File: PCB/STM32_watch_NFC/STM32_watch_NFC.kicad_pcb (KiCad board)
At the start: 4 copper layers, 40 x 40 mm, 107 parts, among them J1 Conn_01x06_Socket, J2 USB_C_Receptacle_PowerOnly_6P, Q1 2N7000, SW1 SW_DPST_x2, SW2 SW_DPST_x2, SW3 SW_DPST_x2, U1 STM32L031G6Ux, U2 MIC5365-3.3YC5, U3 ST25R3916-AQWT, U4 MT3608, Y1 27.12Mhz, Y2 32.768kHz

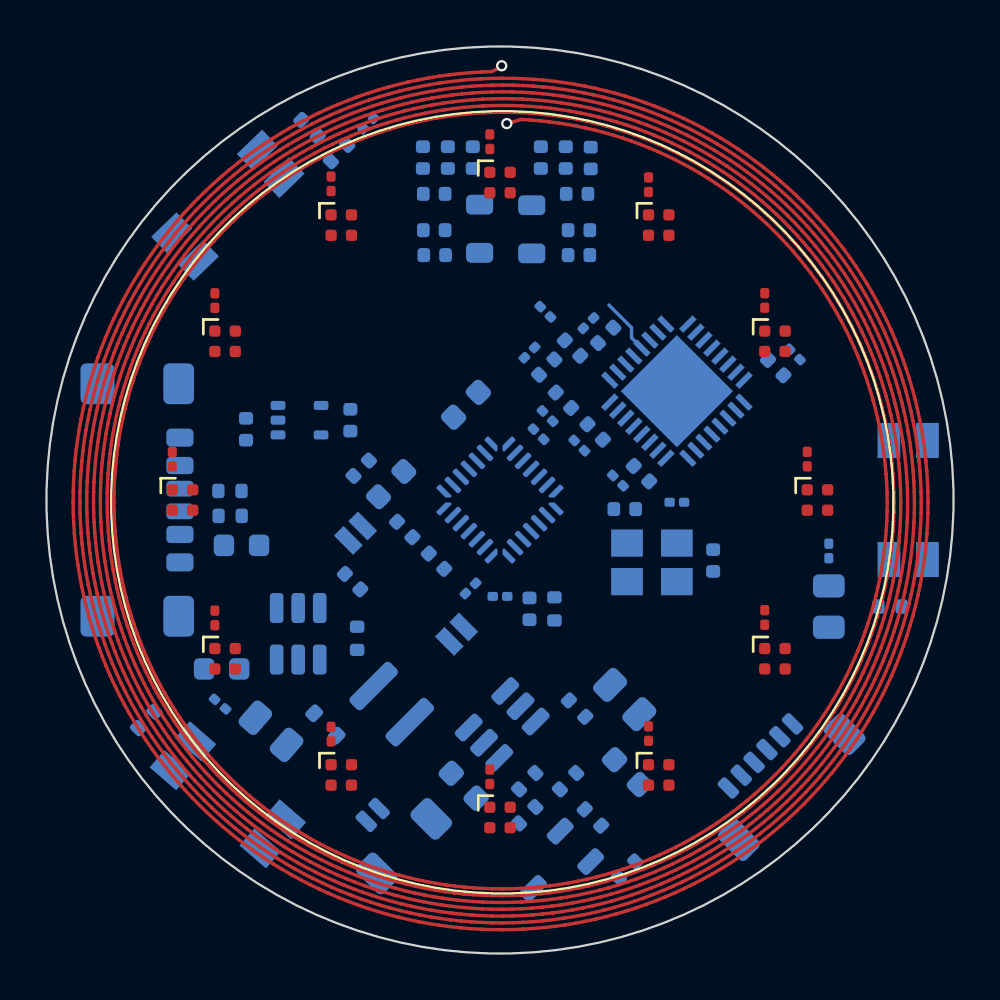
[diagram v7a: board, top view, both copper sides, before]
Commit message: Kicad - Routing 1
Starting routing. I did already a little bitte of routing
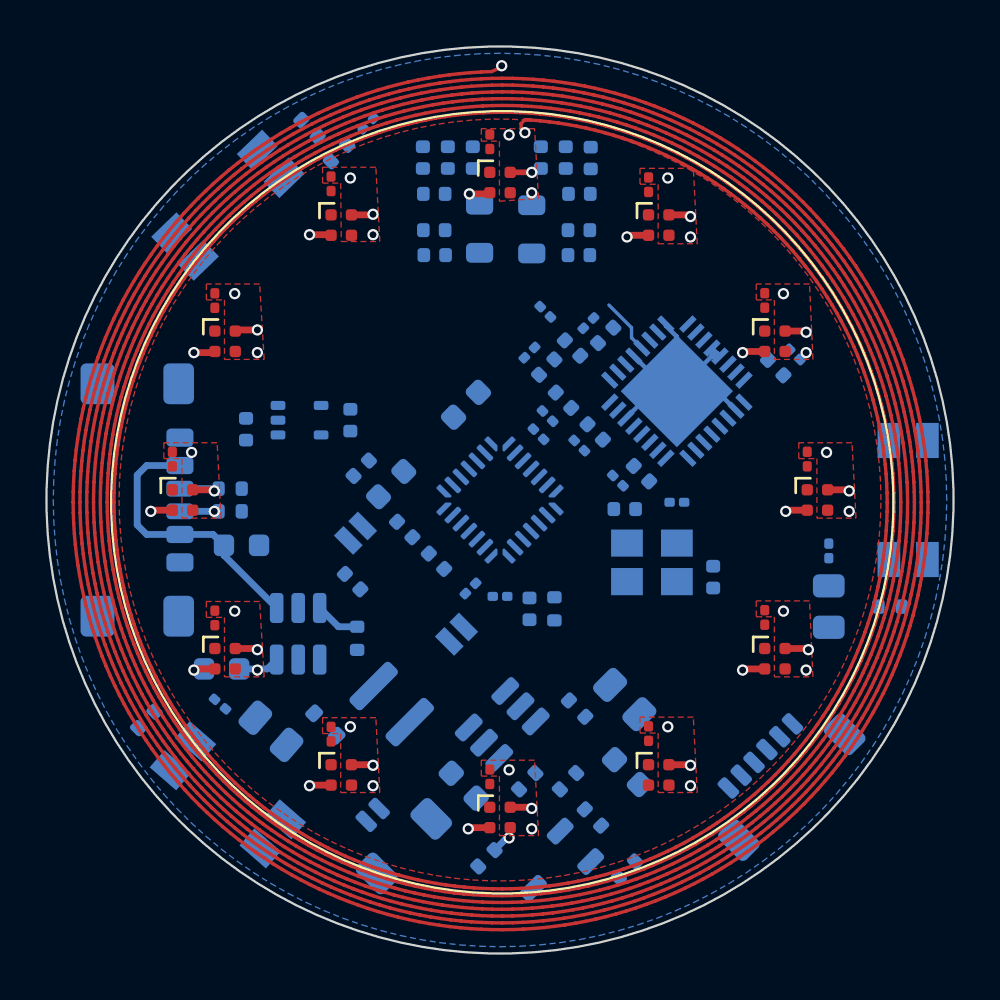
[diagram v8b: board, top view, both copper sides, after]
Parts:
- moved R6 2.62 mm to (147.9, 120.8)
- moved R5 1.20 mm to (136.6, 104.5)
- moved R4 0.90 mm to (136.6, 105.5)
- moved C49 0.73 mm to (157.9, 108.4)
- moved C61 0.10 mm to (152.0, 91.5)
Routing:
- net Net-(D11-DOUT): track 0.00 -> 18.3 mm, vias 0 -> 2
- net GND: track 0.00 -> 15.0 mm, vias 0 -> 24
- net Net-(D10-DOUT): track 0.00 -> 14.2 mm, vias 0 -> 2
- net Net-(D1-DIN): track 0.00 -> 12.8 mm, vias 0 -> 2
- net Net-(D10-DIN): track 0.00 -> 12.8 mm, vias 0 -> 2
- net VBUS: track 0.00 -> 12.2 mm
- net Net-(D1-DOUT): track 0.00 -> 12.1 mm, vias 0 -> 2
- net Net-(D2-DOUT): track 0.00 -> 11.6 mm, vias 0 -> 2
- net Net-(D3-DOUT): track 0.00 -> 10.5 mm, vias 0 -> 2
- net Net-(D8-DOUT): track 0.00 -> 8.91 mm, vias 0 -> 2
- net Net-(D4-DOUT): track 0.00 -> 8.53 mm, vias 0 -> 2
- net Net-(D7-DOUT): track 0.00 -> 7.29 mm, vias 0 -> 2
- net Net-(D5-DOUT): track 0.00 -> 7.11 mm, vias 0 -> 2
- net Net-(D7-DIN): track 0.00 -> 3.84 mm, vias 0 -> 2
- net Net-(ME4055A1-PROG): track 0.00 -> 1.99 mm
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- added copper zone on F.Cu, net +5V
- added copper zone on B.Cu, net GND
- added copper zone on F.Cu, net GND
